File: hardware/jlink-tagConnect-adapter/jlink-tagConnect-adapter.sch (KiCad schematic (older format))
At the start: 13 parts, among them J1 Conn_01x07, J2 Conn_01x03, J3 Conn_02x10_Odd_Even, J4 Conn_01x03, J5 Conn_02x05_Odd_Even, J6 Conn_01x03, J7 Conn_01x03, SW1 SW_Push

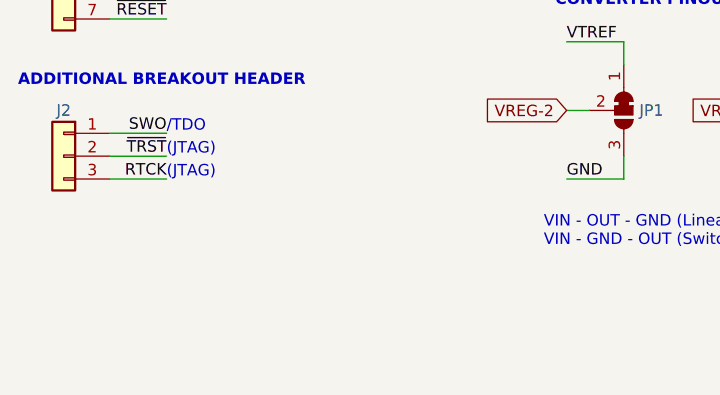
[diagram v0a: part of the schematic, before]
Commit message: Added note to schematic about RTCK connection
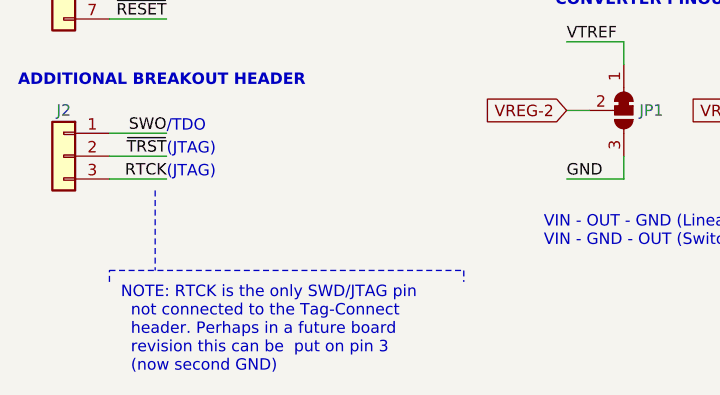
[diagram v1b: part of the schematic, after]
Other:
- note added: "NOTE: RTCK is the only SWD/JTAG pin\n not connected to the Tag-Connect \n header. Perhaps in a future board\n revision this can be put on pin 3\n (now second GND)"
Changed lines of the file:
@@
 Text Notes 3650 4200 0    50   ~ 0
 (not plugged in = disabled)
+Text Notes 1700 6600 0    50   ~ 0
+NOTE: RTCK is the only SWD/JTAG pin\n  not connected to the Tag-Connect \n  header. Perhaps in a future board\n  revision this can be  put on pin 3\n  (now second GND)
+Wire Notes Line
+	1650 6200 1650 6150
+Wire Notes Line
+	1650 6150 3200 6150
+Wire Notes Line
+	3200 6150 3200 6200
+Wire Notes Line
+	1850 5800 1850 6150
 $EndSCHEMATC
